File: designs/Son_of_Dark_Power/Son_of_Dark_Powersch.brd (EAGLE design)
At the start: 89.4 x 55.5 mm, 74 parts, among them IC2 TS5205, J1 22-05-7048-04, J2 22-05-7028-02, J3 22-05-7028-02, J4 22-05-7028-02, J5 22-05-7028-02, J6 22-05-7028-02, J7 22-05-7028-02, J8 22-05-7028-02, J9 22-05-7028-02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

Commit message: servo cape
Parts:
- R1: value (none) -> 0 ohm

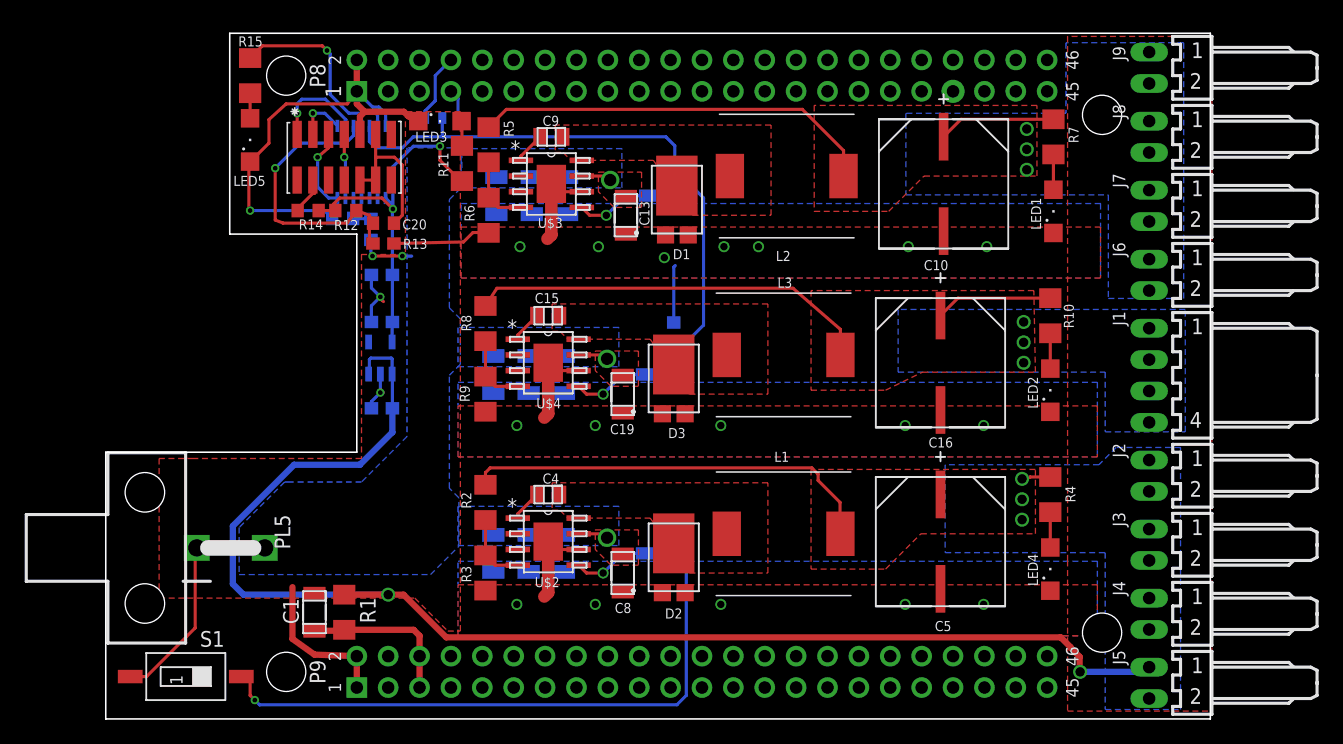
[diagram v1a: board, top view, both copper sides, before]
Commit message: Need to add switch
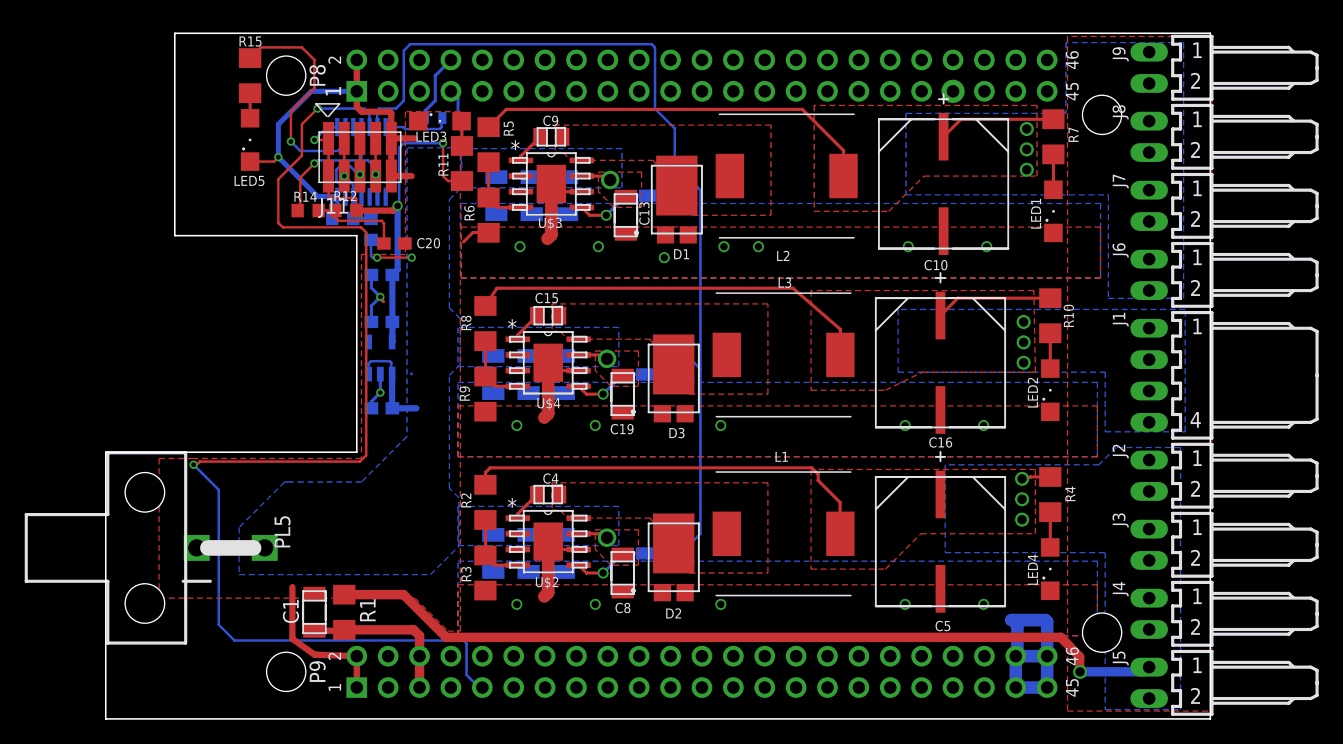
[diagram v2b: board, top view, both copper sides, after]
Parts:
- removed R13: 220, rcl:R0603
- removed R20: 49.9k, rcl:R0603
- removed S1: POWER ON, smd-special:SMS-001
- removed U$12: DEBUG_CON, range_cape:DEBUG_SM
- removed U$5: MSP430F20X3, TIparts:TSSOP-14
- added J11: PIN-CONNECTOR74089, Mother-Board-rev5:10-PIN-SMD
- added U$6: PIC16F676-I/ST, Microchip_By_element14_Batch_1:SOP65P640X120-14N
- moved C20 0.89 mm to (23.4, 37.8)
- turned R12 to 0 degrees
- turned R14 to 180 degrees
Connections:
- removed net LDS_RX: U$1.P9.24
- removed net LDS_TX: U$1.P9.26
- removed net LIDAR_DIR: U$1.P9.23
- removed net LIDAR_PWM: U$1.P9.22
- removed net N$11: C21.1, C22.1, IC2.5, R11.2, R12.2, R14.2, U$5.1
- removed net POWER_EN: Q2.1, S1.2
- removed net RESET: C20.1, R12.1, R13.2, U$5.10
- removed net SCL: U$1.P9.19
- removed net SDA: U$1.P9.20
- removed net SIMO: U$1.P9.30
- removed net SOMI: U$1.P9.29
- removed net SPI_CLK: U$1.P9.31
- removed net SPI_SL0: U$1.P9.28
- removed net SPI_SL1: U$1.P9.42
- removed net TCK: U$12.7, U$5.6
- removed net TDI/VPP: U$12.3, U$5.8
- removed net TDO/TDI: U$12.1, U$5.9
- removed net TEST/VPP: U$5.11
- removed net TMS: U$12.5, U$5.7
- new net +3V3: C21.1, C22.1, IC2.5, J11.1, J11.2, R11.2, R12.2, U$6.1
- new net BB_PWR_SW: U$1.P9.9, U$6.5
- new net ICSPCLK: J11.3, J11.4, U$6.12
- new net ICSPDAT: J11.5, J11.6, U$6.13
- new net N$15: U$6.9
- new net N$16: U$6.10
- new net N$17: U$6.3
- new net POWER_SIG: SPDT.2, U$6.7
- new net VPP/MCLR: J11.7, J11.8, R14.2, U$6.4
- net +5V: no longer C23.1, IC2.1, IC2.3
- net EN: now also Q2.1, U$6.6; no longer R20.2, SPDT.2, U$5.12
- net GND: now also J11.10, J11.9, U$1.P9.43, U$1.P9.44, U$1.P9.45, U$1.P9.46, U$6.14; no longer R20.1, S1.1, U$12.9, U$5.14
- net N$5: now also U$6.8; no longer R13.1, U$12.10, U$12.11, U$12.12
- net N$6: now also C20.1, R12.1; no longer U$12.4
- net N$8: now also U$6.11; no longer U$5.5
- net N$9: now also U$6.2; no longer U$5.13
- net VCC: now also C23.1, IC2.1, IC2.3
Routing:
- net BB_PWR_SW: track 0.00 -> 94.5 mm, vias 0 -> 2
- net POWER_EN: track 51.5 -> 0.00 mm, vias 1 -> 0
- net +5V: track 147.7 -> 105.0 mm, vias 5 -> 4
- net +3V3: track 0.00 -> 38.9 mm, vias 0 -> 3
- net N$11: track 30.9 -> 0.00 mm, vias 2 -> 0
- net EN: track 49.3 -> 75.5 mm
- net RESET: track 23.8 -> 0.00 mm, vias 1 -> 0
- net VPP/MCLR: track 0.00 -> 15.9 mm, vias 0 -> 2
- net N$5: track 12.4 -> 0.00 mm
- net VCC: track 11.8 -> 20.5 mm
- net ICSPDAT: track 0.00 -> 8.05 mm, vias 0 -> 1
- net TDO/TDI: track 7.77 -> 0.00 mm, vias 1 -> 0
- net TMS: track 6.65 -> 0.00 mm, vias 1 -> 0
- net GND: track 106.0 -> 99.5 mm
- net POWER_SIG: track 0.00 -> 5.43 mm
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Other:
- outline, holes or cut-outs redrawn

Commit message: Done with rev 2
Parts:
- added POWER: SPST-2_5X4, ultrasonic_mount:SPST-TAC-4X2_5MM
- moved LED5 6.45 mm to (7.87, 51.4), turned to 270 degrees
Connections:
- removed net N$17: U$6.3
- new net N$11: POWER.P$1, U$6.3
- net GND: now also POWER.P$2
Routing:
- net N$11: track 0.00 -> 18.0 mm, vias 0 -> 3
- net GND: track 99.5 -> 116.8 mm
- net N$10: track 2.03 -> 4.14 mm
- net N$9: track 20.6 -> 19.3 mm
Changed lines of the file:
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@@
 <?xml version="1.0" encoding="utf-8"?>
 <!DOCTYPE eagle SYSTEM "eagle.dtd">
-<eagle version="7.4.0">
+<eagle version="7.3.0">
 <drawing>
 <settings>
@@
 <attribute name="VENDOR" value="TDK" x="16.891" y="2.921" size="1.778" layer="27" rot="R90" display="off"/>
 <attribute name="NAME" x="15.621" y="7.0358" size="1.27" layer="25" ratio="6" rot="SR90"/>
-<attribute name="VALUE" x="16.637" y="-6.3754" size="1.27" layer="27" ratio="6" rot="SR90"/>
 </element>
 <element name="R1" library="rcl" package="R1206" value="0 ohm" x="19.304" y="8.001" smashed="yes" rot="R90">
@@
 <attribute name="NAME" x="12.7" y="54.61" size="0.8128" layer="25" rot="R180"/>
 </element>
-<element name="LED5" library="led" package="SML1206" value="" x="11.684" y="46.228" smashed="yes" rot="R90">
-<attribute name="NAME" x="12.93" y="43.323" size="0.8128" layer="25" rot="R180"/>
-<attribute name="VALUE" x="14.184" y="44.728" size="1.27" layer="27" rot="R90"/>
+<element name="LED5" library="led" package="SML1206" value="" x="7.874" y="51.435" smashed="yes" rot="R270">
+<attribute name="NAME" x="6.628" y="54.34" size="0.8128" layer="25"/>
+<attribute name="VALUE" x="5.374" y="52.935" size="1.27" layer="27" rot="R270"/>
 </element>
 <element name="SPDT" library="range_cape" package="SPDT" value="SPDT_SWITCH" x="27.813" y="48.006" smashed="yes" rot="MR0"/>
@@
 </element>
 <element name="J11" library="Mother-Board-rev5" package="10-PIN-SMD" value="PIN-CONNECTOR74089" x="20.574" y="44.831"/>
+<element name="POWER" library="ultrasonic_mount" package="SPST-TAC-4X2_5MM" value="SPST-2_5X4" x="8.255" y="41.656" smashed="yes" rot="R90">
+<attribute name="NAME" x="6.731" y="40.386" size="0.6096" layer="25" font="vector" rot="R90"/>
+</element>
 </elements>
 <signals>
@@
 <wire x1="16.637" y1="50.165" x2="20.32" y2="50.165" width="0.4064" layer="16"/>
 <contactref element="LED5" pad="C"/>
-<wire x1="11.684" y1="44.478" x2="13.617" y2="44.478" width="0.2032" layer="1"/>
 <wire x1="13.617" y1="44.478" x2="13.97" y2="44.831" width="0.2032" layer="1"/>
 <via x="13.97" y="44.831" extent="1-16" drill="0.381"/>
@@
 <wire x1="73.787" y1="6.985" x2="73.787" y2="4.572" width="1.016" layer="16"/>
 <wire x1="73.787" y1="4.572" x2="73.66" y2="4.445" width="1.016" layer="16"/>
+<contactref element="POWER" pad="P$2"/>
+<wire x1="7.874" y1="53.185" x2="6.83" y2="53.185" width="0.2032" layer="1"/>
+<wire x1="6.83" y1="53.185" x2="6.35" y2="52.705" width="0.2032" layer="1"/>
+<wire x1="6.35" y1="52.705" x2="6.35" y2="44.861" width="0.2032" layer="1"/>
+<wire x1="6.733" y1="44.478" x2="8.255" y2="42.956" width="0.2032" layer="1"/>
+<wire x1="13.617" y1="44.478" x2="6.733" y2="44.478" width="0.2032" layer="1"/>
+<wire x1="6.733" y1="44.478" x2="6.35" y2="44.861" width="0.2032" layer="1"/>
 </signal>
 <signal name="N$1">
@@
 <contactref element="R15" pad="1"/>
 <contactref element="LED5" pad="A"/>
-<wire x1="11.684" y1="50.013" x2="11.684" y2="47.978" width="0.254" layer="1"/>
+<wire x1="11.684" y1="50.013" x2="7.874" y2="50.013" width="0.2032" layer="1"/>
+<wire x1="7.874" y1="50.013" x2="7.874" y2="49.685" width="0.2032" layer="1"/>
 </signal>
 <signal name="N$9">
 <contactref element="R15" pad="2"/>
 <contactref element="U$6" pad="2"/>
-<wire x1="19.4056" y1="47.2694" x2="19.4056" y2="45.9486" width="0.2032" layer="16"/>
-<wire x1="19.4056" y1="45.9486" x2="18.796" y2="45.339" width="0.2032" layer="16"/>
-<wire x1="18.796" y1="45.339" x2="15.748" y2="45.339" width="0.2032" layer="16"/>
-<wire x1="15.748" y1="45.339" x2="14.986" y2="46.101" width="0.2032" layer="16"/>
-<via x="14.986" y="46.101" extent="1-16" drill="0.381"/>
-<wire x1="14.986" y1="46.101" x2="14.986" y2="48.514" width="0.2032" layer="1"/>
+<via x="14.986" y="46.736" extent="1-16" drill="0.381"/>
+<wire x1="14.986" y1="46.736" x2="14.986" y2="48.514" width="0.2032" layer="1"/>
 <wire x1="14.986" y1="48.514" x2="16.891" y2="50.419" width="0.2032" layer="1"/>
 <wire x1="16.891" y1="52.705" x2="15.875" y2="53.721" width="0.2032" layer="1"/>
@@
 <wire x1="15.875" y1="53.721" x2="12.548" y2="53.721" width="0.2032" layer="1"/>
 <wire x1="12.548" y1="53.721" x2="11.684" y2="52.857" width="0.2032" layer="1"/>
+<wire x1="19.4056" y1="47.2694" x2="19.4056" y2="46.3296" width="0.2032" layer="16"/>
+<wire x1="19.4056" y1="46.3296" x2="19.177" y2="46.101" width="0.2032" layer="16"/>
+<wire x1="19.177" y1="46.101" x2="15.621" y2="46.101" width="0.2032" layer="16"/>
+<wire x1="15.621" y1="46.101" x2="14.986" y2="46.736" width="0.2032" layer="16"/>
 </signal>
 <signal name="N$12">
@@
 <wire x1="18.034" y1="43.307" x2="18.034" y2="46.355" width="0.2032" layer="1"/>
 <wire x1="18.034" y1="46.355" x2="17.907" y2="46.228" width="0.2032" layer="1"/>
-<wire x1="17.907" y1="46.228" x2="16.891" y2="46.228" width="0.2032" layer="1"/>
-<via x="16.891" y="46.228" extent="1-16" drill="0.381"/>
-<wire x1="16.891" y1="46.228" x2="17.9324" y2="47.2694" width="0.2032" layer="16"/>
-<wire x1="17.9324" y1="47.2694" x2="18.7452" y2="47.2694" width="0.2032" layer="16"/>
+<via x="16.891" y="47.244" extent="1-16" drill="0.381"/>
 <wire x1="20.281" y1="40.513" x2="20.281" y2="41.441" width="0.2032" layer="1"/>
 <wire x1="20.281" y1="41.441" x2="20.193" y2="41.529" width="0.2032" layer="1"/>
@@
 <wire x1="23.749" y1="45.593" x2="23.749" y2="41.021" width="0.2032" layer="16"/>
 <wire x1="23.749" y1="41.021" x2="23.622" y2="40.894" width="0.2032" layer="16"/>
+<wire x1="18.7452" y1="47.2694" x2="16.9164" y2="47.2694" width="0.2032" layer="16"/>
+<wire x1="16.9164" y1="47.2694" x2="16.891" y2="47.244" width="0.2032" layer="16"/>
+<wire x1="16.891" y1="47.244" x2="17.145" y2="47.244" width="0.2032" layer="1"/>
+<wire x1="17.145" y1="47.244" x2="18.034" y2="46.355" width="0.2032" layer="1"/>
 </signal>
 <signal name="VPP/MCLR">
@@
 <wire x1="15.875" y1="47.498" x2="17.145" y2="48.768" width="0.2032" layer="1"/>
 <via x="17.145" y="48.768" extent="1-16" drill="0.381"/>
-<wire x1="17.145" y1="48.768" x2="20.955" y2="48.768" width="0.2032" layer="16"/>
 <wire x1="20.955" y1="48.768" x2="21.336" y2="48.387" width="0.2032" layer="16"/>
 <wire x1="21.336" y1="48.387" x2="21.336" y2="47.2948" width="0.2032" layer="16"/>
 <wire x1="21.336" y1="47.2948" x2="21.3614" y2="47.2694" width="0.2032" layer="16"/>
 <wire x1="21.082" y1="38.735" x2="20.6629" y2="39.1541" width="0.2032" layer="1"/>
+<wire x1="20.955" y1="48.768" x2="17.145" y2="48.768" width="0.2032" layer="16"/>
 </signal>
 <signal name="N$15">
@@
 <signal name="N$16">
 <contactref element="U$6" pad="10"/>
-</signal>
-<signal name="N$17">
-<contactref element="U$6" pad="3"/>
 </signal>
 <signal name="POWER_SIG">
@@
 <contactref element="U$6" pad="8"/>
 </signal>
+<signal name="N$11">
+<contactref element="U$6" pad="3"/>
+<contactref element="POWER" pad="P$1"/>
+<wire x1="20.0406" y1="47.2694" x2="20.0406" y2="45.9486" width="0.2032" layer="16"/>
+<wire x1="20.0406" y1="45.9486" x2="19.685" y2="45.593" width="0.2032" layer="16"/>
+<wire x1="19.685" y1="45.593" x2="14.986" y2="45.593" width="0.2032" layer="16"/>
+<via x="14.986" y="45.593" extent="1-16" drill="0.381"/>
+<wire x1="14.986" y1="45.593" x2="11.43" y2="45.593" width="0.2032" layer="1"/>
+<via x="11.43" y="45.593" extent="1-16" drill="0.381"/>
+<wire x1="11.43" y1="45.593" x2="11.43" y2="43.561" width="0.2032" layer="16"/>
+<via x="11.43" y="43.561" extent="1-16" drill="0.381"/>
+<wire x1="11.43" y1="43.561" x2="11.43" y2="41.275" width="0.2032" layer="1"/>
+<wire x1="11.43" y1="41.275" x2="10.541" y2="40.386" width="0.2032" layer="1"/>
+<wire x1="10.541" y1="40.386" x2="8.285" y2="40.386" width="0.2032" layer="1"/>
+<wire x1="8.285" y1="40.386" x2="8.255" y2="40.356" width="0.2032" layer="1"/>
+</signal>
 </signals>
